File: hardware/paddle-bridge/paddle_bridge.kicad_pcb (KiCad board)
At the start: 2 copper layers, 44.5 x 35.7 mm, 15 parts, among them J1 APOLLO (P4 header GND,52,51,5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, J2 MACHINE: paddle + Micra white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, U1 AQY212EH, U2 LH1502BB, U3 LH1502BB

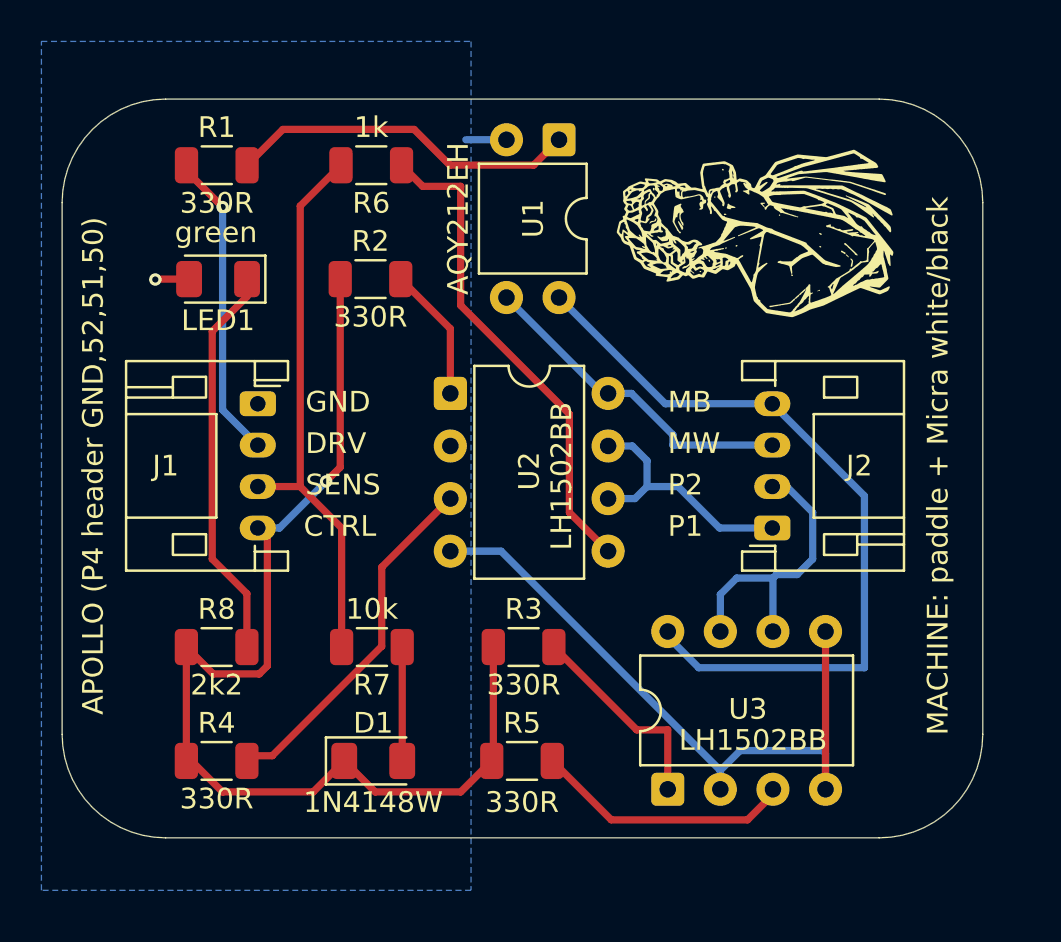
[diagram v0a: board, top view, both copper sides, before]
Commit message: hardware: Apollo Link rev 0.6 - USB-C 5 V in, powers the Apollo over J1; gerbers + BOM
The bridge now carries a 5 V rail so a single 5-conductor cable can power
the remote through the P4's 40-pin header instead of a second USB lead:

- J3: GCT USB4085-GF-A USB-C receptacle (THT), power only. R9/R10 5k1 Rd
  on CC1/CC2 so any USB-C source, PD or not, turns VBUS on at 5 V.
- F1: 1.5 A hold / 3 A trip PTC (Littelfuse 1812L150/12DR) between VBUS
  and the 5V net; the Apollo peaks at ~0.6 A, and the hold current still
  clears that at the 85 C in-chassis limit. VBUS/5V tracks 0.5 mm.
- J1 grows from S4B-PH-K to S5B-PH-K: GND_R / 5V / DRIVE / SENSE / CTRL.
- No-connect flags on D+/D-/SBU; ERC clean apart from the 'bridge' library
  path warnings. DRC: only the USB4085 footprint's inherent 0.15 mm
  pad-to-pad gaps and the edge-clipped silk at the receptacle remain.
- Title blocks, sheet notes and bottom silk at rev 0.6 / 2026-09-24.
- BOM: 13 Mouser line items; the rev 0.5 gerber zip is kept alongside.
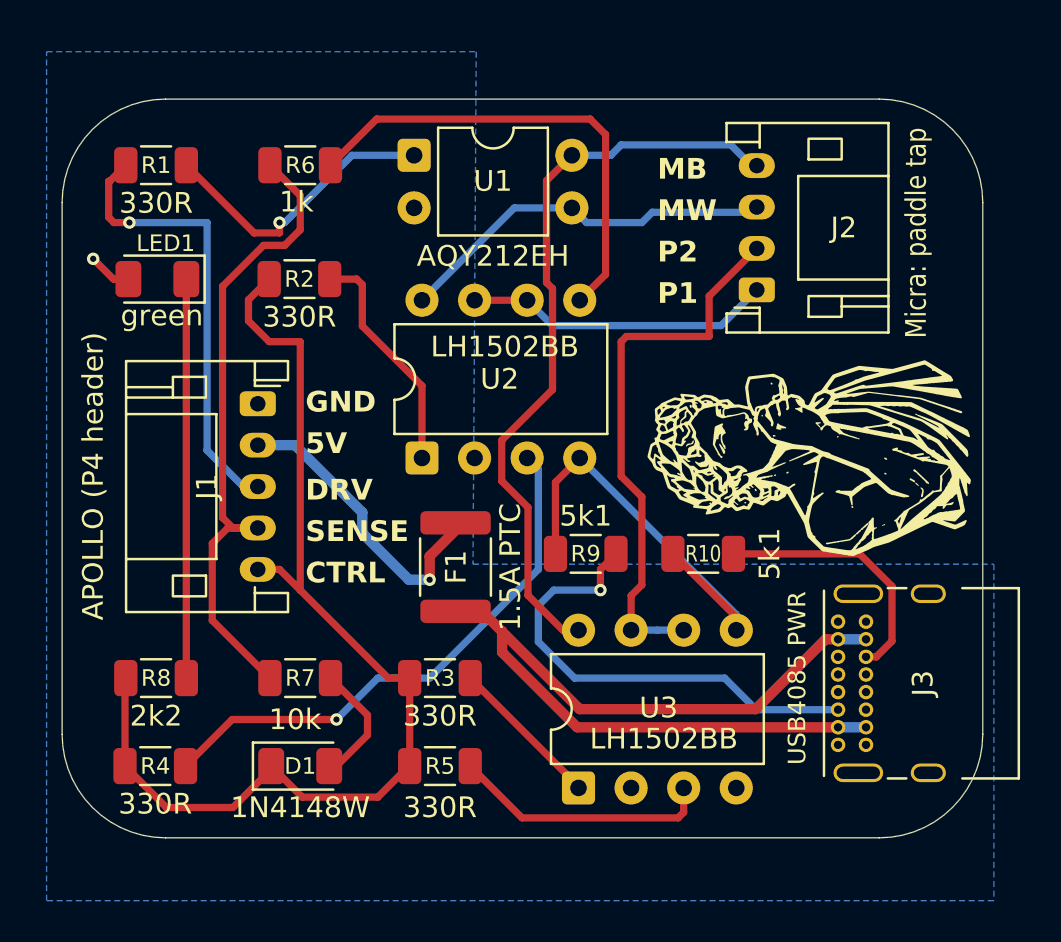
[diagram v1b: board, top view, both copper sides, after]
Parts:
- added F1: 1.5A PTC, Fuse:Fuse_1812_4532Metric, F.Cu at (137.5, 84.9)
- added J3: USB4085 PWR, Connector_USB:USB_C_Receptacle_GCT_USB4085, F.Cu at (156.0, 93.5)
- added R10: 5k1, Resistor_SMD:R_1206_3216Metric, F.Cu at (149.5, 84.2)
- added R9: 5k1, Resistor_SMD:R_1206_3216Metric, F.Cu at (143.8, 84.2)
- J1: value APOLLO (P4 header GND,52,51,50) -> APOLLO (P4 header); footprint Connector_JST:JST_PH_S4B-PH-K_1x04_P2.00mm_Horizontal -> Connector_JST:JST_PH_S5B-PH-K_1x05_P2.00mm_Horizontal
- J2: value MACHINE: paddle + Micra white/black -> Micra: paddle tap
- moved J2 11.5 mm to (152.1, 71.5)
- moved U1 7.04 mm to (135.5, 65.0), turned to 0 degrees
- moved U3 4.31 mm to (143.4, 95.6)
- moved R3 4.31 mm to (136.8, 90.2)
- moved R5 3.97 mm to (136.8, 94.5)
- moved R7 3.77 mm to (130.0, 90.2)
- moved D1 3.53 mm to (130.0, 94.5)
- moved R2 3.43 mm to (130.0, 71.0)
- moved R6 3.43 mm to (130.0, 65.5)
- moved U2 3.41 mm to (135.9, 79.6), turned to 90 degrees
- moved R8 3.29 mm to (123.0, 90.2)
- moved R4 2.97 mm to (123.0, 94.5)
- moved LED1 2.93 mm to (123.1, 71.0)
- moved R1 2.93 mm to (123.0, 65.5)
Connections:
- J1 pad 2: /DRIVE -> /5V
- J1 pad 3: /SENSE -> /DRIVE
- J1 pad 4: /CTRL -> /SENSE
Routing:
- net /VBUS: track 0.00 -> 43.3 mm
- net Net-(J3-CC1): track 0.00 -> 23.0 mm, vias 0 -> 1
- net /5V: track 0.00 -> 14.5 mm, vias 0 -> 1
- net /GND_R: track 37.3 -> 23.6 mm
- net Net-(J3-CC2): track 0.00 -> 12.5 mm
- net /P2: track 14.8 -> 26.7 mm
- net Net-(U2-A2): track 17.2 -> 26.6 mm, vias 0 -> 1
- net /DRIVE: track 14.9 -> 21.9 mm
- net /SENSE: track 27.0 -> 31.8 mm
- net Net-(U2-A1): track 6.51 -> 11.2 mm
- net Net-(U3-A1): track 10.3 -> 7.47 mm
- net Net-(U1-A): track 17.0 -> 14.5 mm, vias 0 -> 1
- net /MICRA_W: track 16.1 -> 18.5 mm
- net /P1: track 12.4 -> 14.9 mm
- net /CTRL: track 53.9 -> 52.1 mm, vias 1 -> 0
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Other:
- board text added: "5V"
- board text added: "SENSE"
- board text removed: "SENS"
